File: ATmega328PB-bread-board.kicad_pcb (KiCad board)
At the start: 2 copper layers, 60 x 60 mm, 10 parts, among them J1 Conn_01x17, J2 Conn_01x17, U1 ATmega328PB-MU

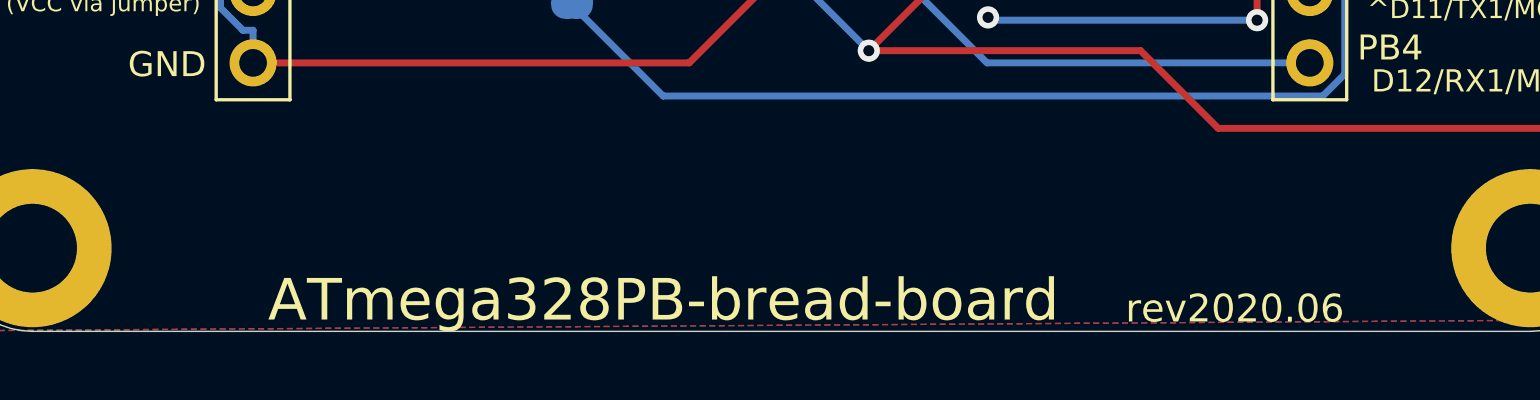
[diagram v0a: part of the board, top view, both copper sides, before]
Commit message: Add size info to pcb
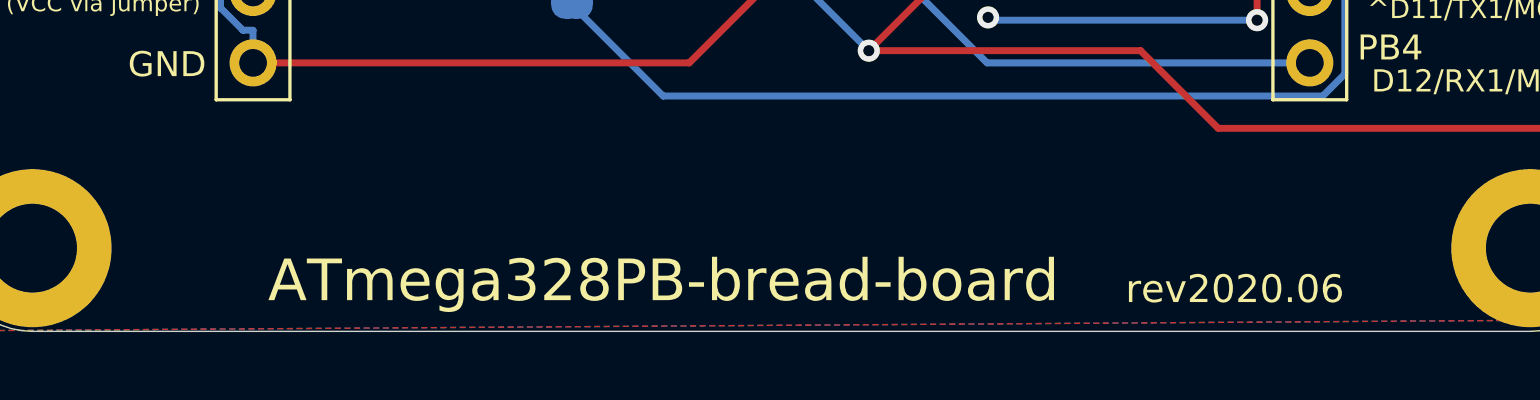
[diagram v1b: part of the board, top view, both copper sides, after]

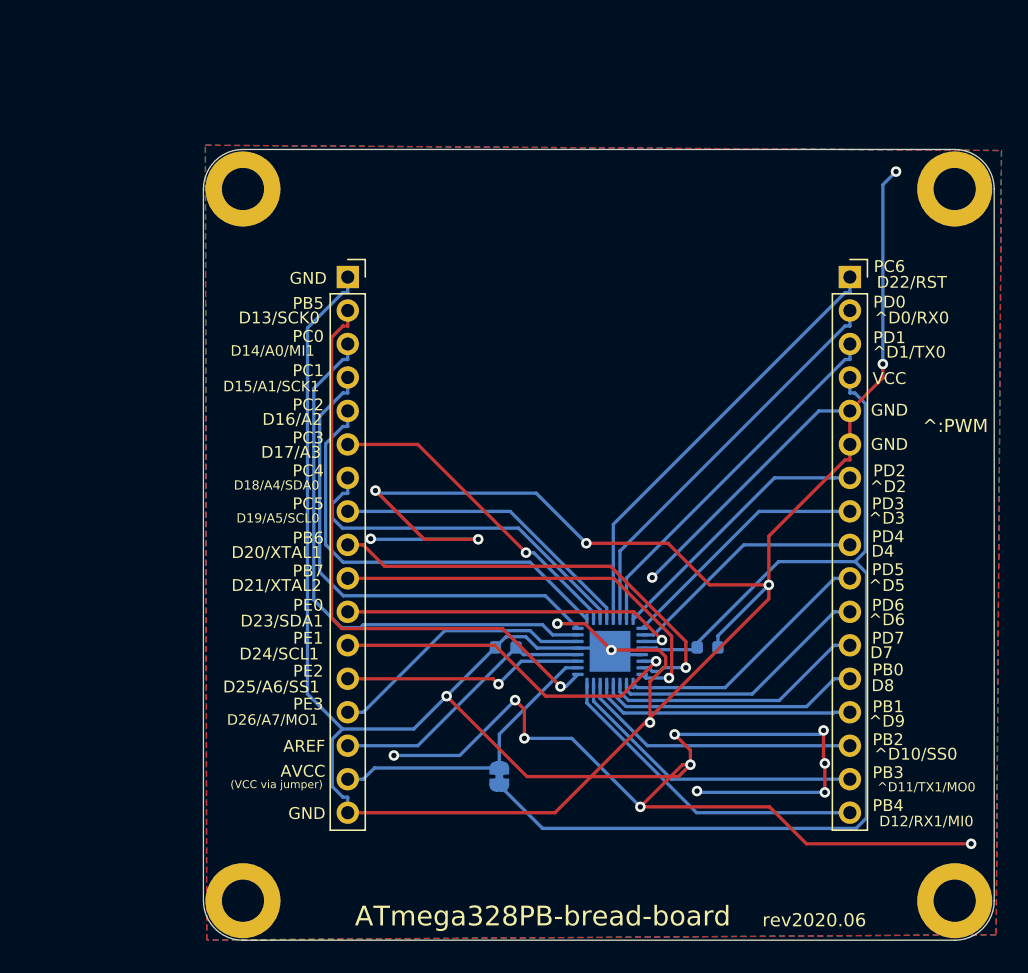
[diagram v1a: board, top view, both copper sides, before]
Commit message: Add DTR pin and change pin layout
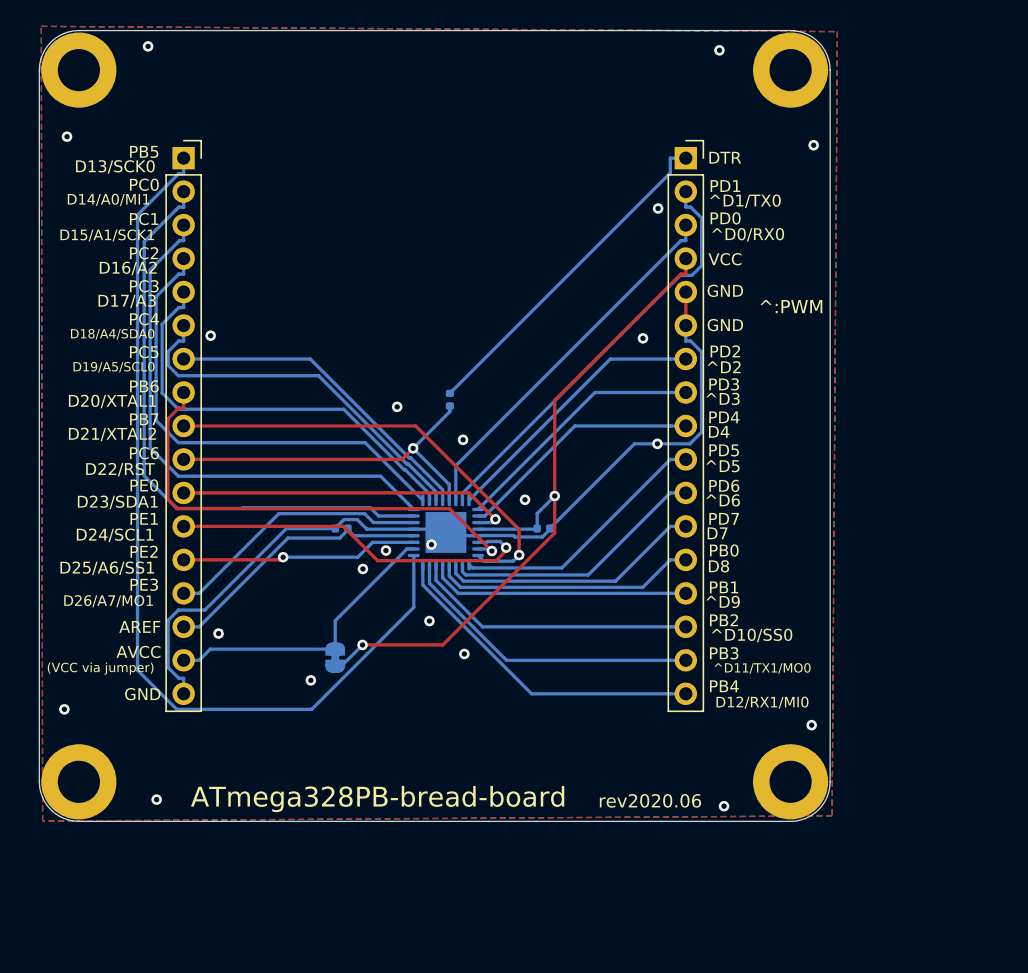
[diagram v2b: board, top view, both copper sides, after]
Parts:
- added C3: 0.1uf, Capacitor_SMD:C_0402_1005Metric, B.Cu at (131.2, 78.0)
- C1: footprint Capacitor_SMD:C_0603_1608Metric -> Capacitor_SMD:C_0402_1005Metric
- C2: value 10uf -> 0.1uf; footprint Capacitor_SMD:C_0603_1608Metric -> Capacitor_SMD:C_0402_1005Metric
- moved U1 15.4 mm to (130.8, 88.1)
- moved J2 15.4 mm to (111.0, 59.7)
- moved REF4 15.4 mm to (103.0, 53.0)
- moved C1 15.4 mm to (122.9, 87.8)
- moved JP1 15.4 mm to (122.5, 97.6)
- moved REF1 15.4 mm to (103.0, 107.0)
- moved J1 15.4 mm to (149.1, 59.7)
- moved REF3 15.4 mm to (157.0, 53.0)
- moved C2 15.4 mm to (138.2, 87.8)
- moved REF2 15.4 mm to (157.0, 107.0)
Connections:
- J1 pad 1: /pc6 -> /DTR
- J1 pad 2: /pd0 -> /pd1
- J1 pad 3: /pd1 -> /pd0
- J2 pad 1: GND -> /pb5
- J2 pad 10: /pb7 -> /pc6
- J2 pad 2: /pb5 -> /pc0
- J2 pad 3: /pc0 -> /pc1
- J2 pad 4: /pc1 -> /pc2
- J2 pad 5: /pc2 -> /pc3
- J2 pad 6: /pc3 -> /pc4
- J2 pad 7: /pc4 -> /pc5
- J2 pad 8: /pc5 -> /pb6
- J2 pad 9: /pb6 -> /pb7
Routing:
- net GND: track 344.1 -> 65.2 mm, vias 23 -> 22
- net VCC: track 83.5 -> 53.5 mm, vias 0 -> 2
- net /DTR: track 0.00 -> 25.9 mm
- net /pb5: track 45.3 -> 69.8 mm, vias 1 -> 0
- net /pc3: track 24.4 -> 32.5 mm, vias 1 -> 0
- net /pc6: track 33.6 -> 27.2 mm, vias 0 -> 1
- net /pd1: track 28.1 -> 32.2 mm
- net /pc2: track 33.2 -> 36.1 mm
- net /pc1: track 37.2 -> 40.1 mm
- net /pc0: track 42.0 -> 44.8 mm
- net /pd0: track 30.9 -> 28.3 mm
- net /pb7: track 31.8 -> 34.1 mm
- net /pb6: track 34.2 -> 36.1 mm
- net /pe1: track 27.1 -> 28.4 mm
- net /pc5: track 23.5 -> 24.6 mm
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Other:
- board text added: "DTR"

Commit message: Move position of mouting holes 0.5mm inside
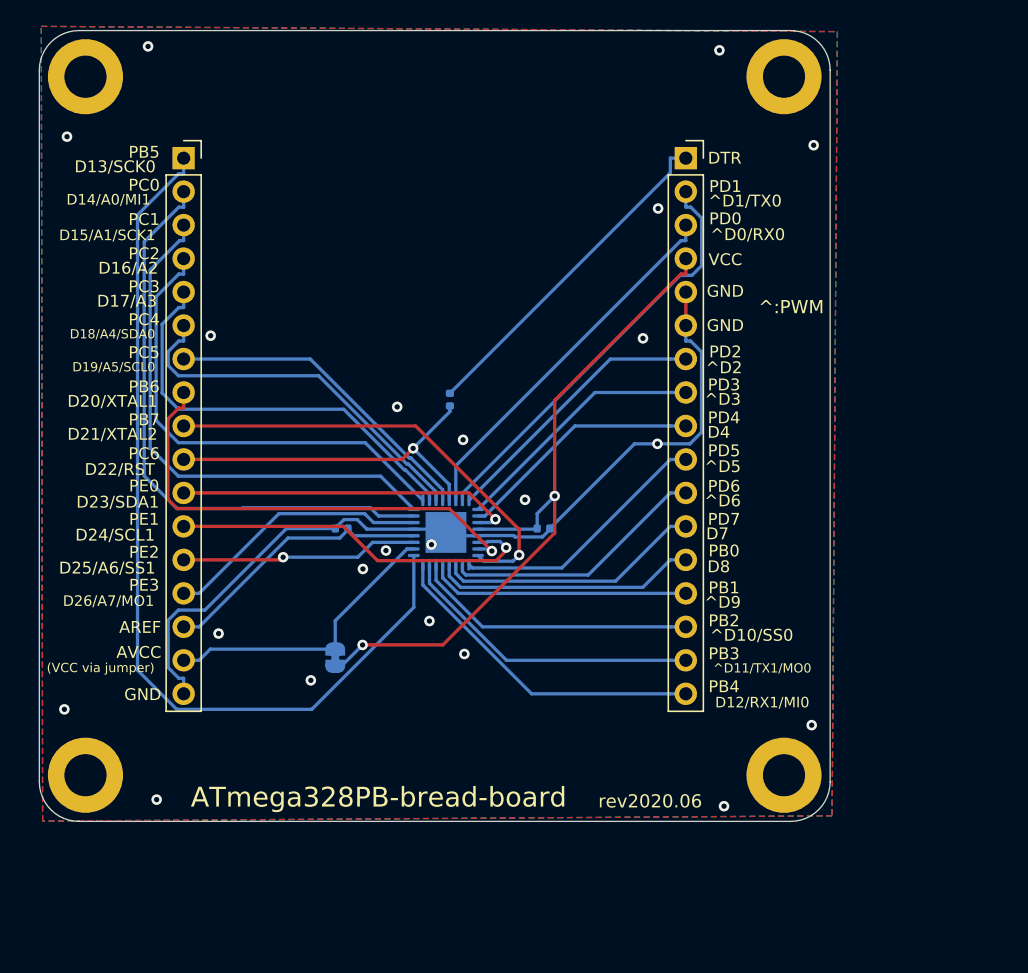
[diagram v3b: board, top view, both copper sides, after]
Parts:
- moved REF1 0.71 mm to (103.5, 106.5)
- moved REF2 0.71 mm to (156.5, 106.5)
- moved REF3 0.71 mm to (156.5, 53.5)
- moved REF4 0.71 mm to (103.5, 53.5)

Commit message: Update revision to 2021.03
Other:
- board text added: "rev2021.03"
- board text removed: "rev2020.06"
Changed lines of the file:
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@@
     (effects (font (size 1 1) (thickness 0.15)))
   )
-  (gr_text rev2020.06 (at 146.35 108.48) (layer F.SilkS)
+  (gr_text rev2021.03 (at 146.35 108.48) (layer F.SilkS)
     (effects (font (size 1 1) (thickness 0.15)))
   )

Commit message: Add pullup resistor to RST
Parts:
- added R1: 10k, Resistor_SMD:R_0603_1608Metric, B.Cu at (134.0, 78.0)
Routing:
- net VCC: track 53.5 -> 58.1 mm, vias 2 -> 3
- net /pc6: track 27.2 -> 29.5 mm
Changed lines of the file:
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@@
   (general
     (thickness 1.6)
-    (drawings 79)
-    (tracks 250)
+    (drawings 80)
+    (tracks 257)
     (zones 0)
-    (modules 11)
+    (modules 12)
     (nets 33)
   )
@@
     (add_net GND)
     (add_net VCC)
+  )
+  (module Resistor_SMD:R_0603_1608Metric (layer B.Cu)
+    (at 134 77.95 180)
+    (descr "Resistor SMD 0603 (1608 Metric), square (rectangular) end terminal, IPC_7351 nominal, (Body size source: IPC-SM-782 page 72, https://www.pcb-3d.com/wordpress/wp-content/uploads/ipc-sm-782a_amendment_1_and_2.pdf), generated with kicad-footprint-generator")
+    (tags resistor)
+    (attr smd)
+    (fp_text reference R1 (at 0 1.43) (layer B.SilkS)
+      (effects (font (size 1 1) (thickness 0.15)) (justify mirror))
+    )
+    (fp_text value 10k (at 0 -1.43) (layer B.Fab)
+      (effects (font (size 1 1) (thickness 0.15)) (justify mirror))
+    )
+    (fp_line (start 1.48 -0.73) (end -1.48 -0.73) (layer B.CrtYd) (width 0.05))
+    (fp_line (start 1.48 0.73) (end 1.48 -0.73) (layer B.CrtYd) (width 0.05))
+    (fp_line (start -1.48 0.73) (end 1.48 0.73) (layer B.CrtYd) (width 0.05))
+    (fp_line (start -1.48 -0.73) (end -1.48 0.73) (layer B.CrtYd) (width 0.05))
+    (fp_line (start -0.237258 -0.5225) (end 0.237258 -0.5225) (layer B.SilkS) (width 0.12))
+    (fp_line (start -0.237258 0.5225) (end 0.237258 0.5225) (layer B.SilkS) (width 0.12))
+    (fp_line (start 0.8 -0.4125) (end -0.8 -0.4125) (layer B.Fab) (width 0.1))
+    (fp_line (start 0.8 0.4125) (end 0.8 -0.4125) (layer B.Fab) (width 0.1))
+    (fp_line (start -0.8 0.4125) (end 0.8 0.4125) (layer B.Fab) (width 0.1))
+    (fp_line (start -0.8 -0.4125) (end -0.8 0.4125) (layer B.Fab) (width 0.1))
+    (fp_text user %R (at 0 0) (layer B.Fab)
+      (effects (font (size 0.4 0.4) (thickness 0.06)) (justify mirror))
+    )
+    (pad 2 smd roundrect (at 0.825 0 180) (size 0.8 0.95) (layers B.Cu B.Paste B.Mask) (roundrect_rratio 0.25)
+      (net 22 /pc6))
+    (pad 1 smd roundrect (at -0.825 0 180) (size 0.8 0.95) (layers B.Cu B.Paste B.Mask) (roundrect_rratio 0.25)
+      (net 3 VCC))
+    (model ${KISYS3DMOD}/Resistor_SMD.3dshapes/R_0603_1608Metric.wrl
+      (at (xyz 0 0 0))
+      (scale (xyz 1 1 1))
+      (rotate (xyz 0 0 0))
+    )
   )
   (module Capacitor_SMD:C_0402_1005Metric (layer B.Cu)
@@
   (via (at 124.5244 96.6136) (size 0.8) (layers F.Cu B.Cu) (net 3))
   (via (at 139.1033 85.313) (size 0.8) (layers F.Cu B.Cu) (net 3))
+  (via (at 135.9 77.6) (size 0.8) (drill 0.4) (layers F.Cu B.Cu) (net 3))
+  (segment (start 135.55 77.95) (end 135.9 77.6) (width 0.25) (layer B.Cu) (net 3))
+  (segment (start 134.825 77.95) (end 135.55 77.95) (width 0.25) (layer B.Cu) (net 3))
+  (segment (start 136.3547 78.0547) (end 139.1033 78.0547) (width 0.25) (layer F.Cu) (net 3))
+  (segment (start 135.9 77.6) (end 136.3547 78.0547) (width 0.25) (layer F.Cu) (net 3))
   (segment (start 129.1 90.5175) (end 129.1 92.0727) (width 0.25) (layer B.Cu) (net 4))
   (segment (start 129.1 92.0727) (end 137.3473 100.32) (width 0.25) (layer B.Cu) (net 4))
@@
   (segment (start 127.5225 82.54) (end 128.3634 81.6991) (width 0.25) (layer F.Cu) (net 22))
   (via (at 128.3634 81.6991) (size 0.8) (layers F.Cu B.Cu) (net 22))
+  (segment (start 132.645 78.48) (end 133.175 77.95) (width 0.25) (layer B.Cu) (net 22))
+  (segment (start 131.15 78.48) (end 132.645 78.48) (width 0.25) (layer B.Cu) (net 22))
   (segment (start 136.4067 89.7929) (end 135.9404 90.2592) (width 0.25) (layer B.Cu) (net 23))
   (segment (start 135.9404 90.2592) (end 133.7167 90.2592) (width 0.25) (layer B.Cu) (net 23))
@@
     (connect_pads (clearance 0.508))
     (min_thickness 0.254)
-    (fill yes (arc_segments 32) (thermal_gap 0.508) (thermal_bridge_width 0.508))
+    (fill (arc_segments 32) (thermal_gap 0.508) (thermal_bridge_width 0.508))
     (polygon
       (pts
@@
     (connect_pads (clearance 0.508))
     (min_thickness 0.254)
-    (fill yes (arc_segments 32) (thermal_gap 0.508) (thermal_bridge_width 0.508))
+    (fill (arc_segments 32) (thermal_gap 0.508) (thermal_bridge_width 0.508))
     (polygon
       (pts
